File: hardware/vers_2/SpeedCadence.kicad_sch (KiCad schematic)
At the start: 30 parts, among them J1 Conn_ST_STDC14, J2 USB_C_Receptacle_USB2.0_16P, J3 Conn_01x03_Pin, J4 Conn_01x02_Pin, J5 Conn_01x04_Pin, SW2 SW_Push, U1 AP2112K-3.3, U2 STM32F103C8Tx, U3 TCAN3414DR, Y1 CSTNE8M00G52Z000R0

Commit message: Revision 2
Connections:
- net OLED_SCL: no longer U2.43 (PB7)
- net OLED_SDA: now also U2.43 (PB7)
- net +5V renamed +LDO_IN
- net +5V_BATT renamed GND
- net GND: no longer BT1.1 (Pin_1), D3.2 (A)
- new net +V_BATT: BT1.1 (Pin_1), D3.2 (A)
- no-connect marks 10 -> 34
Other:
- moved on the sheet: BT1, D1, D2, D3, F1, J2, J3, R1, R2

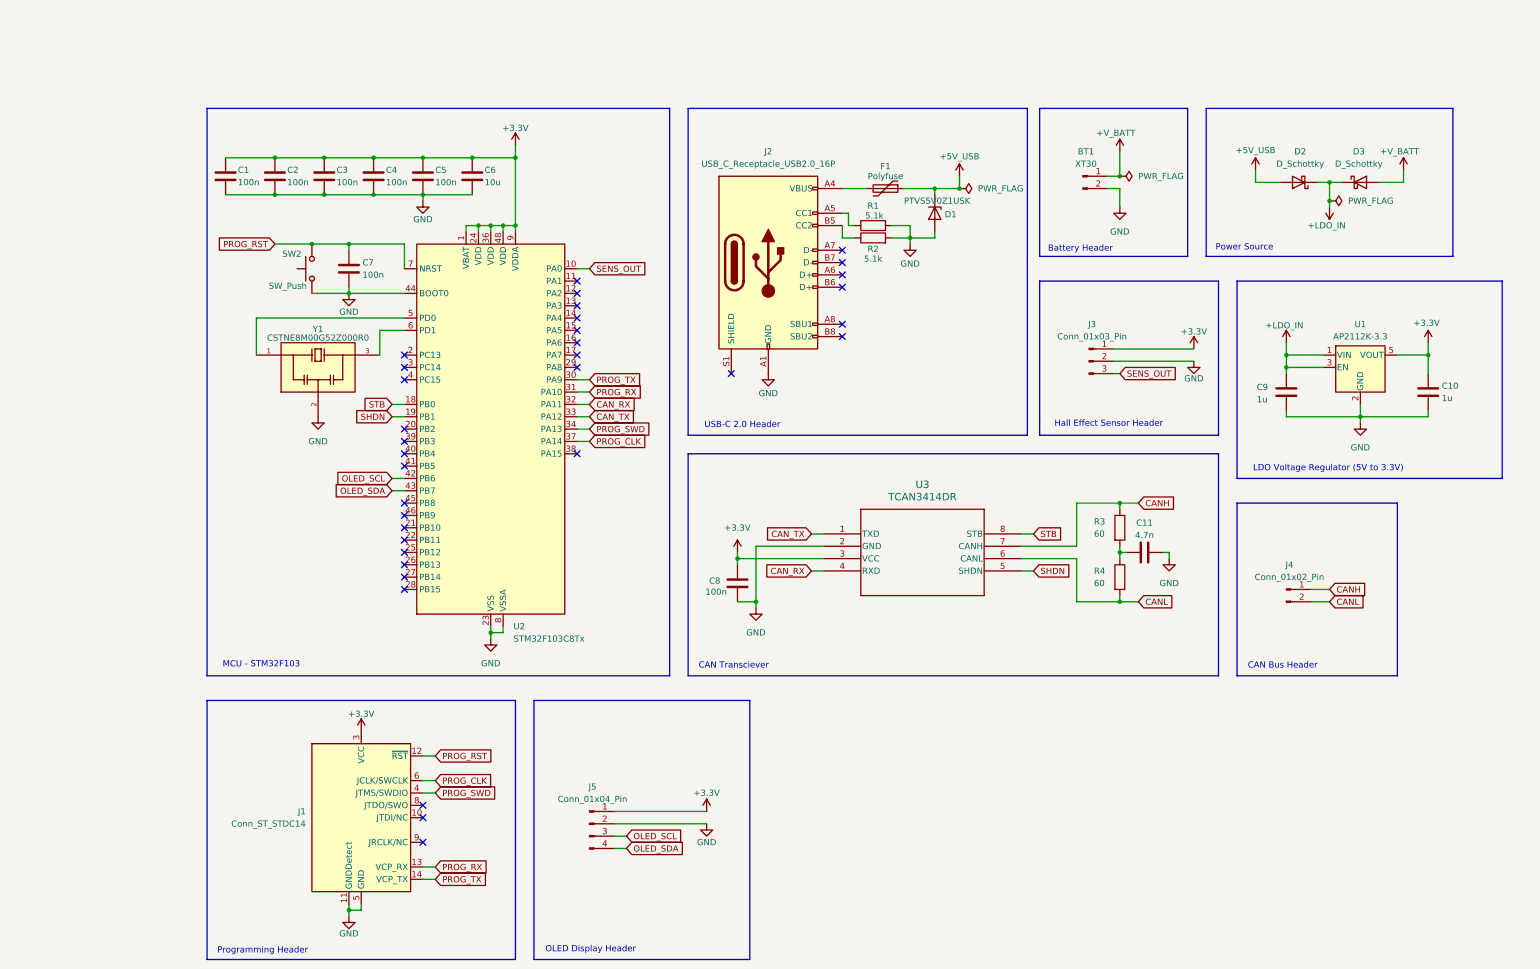
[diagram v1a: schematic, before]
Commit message: Updated LDO
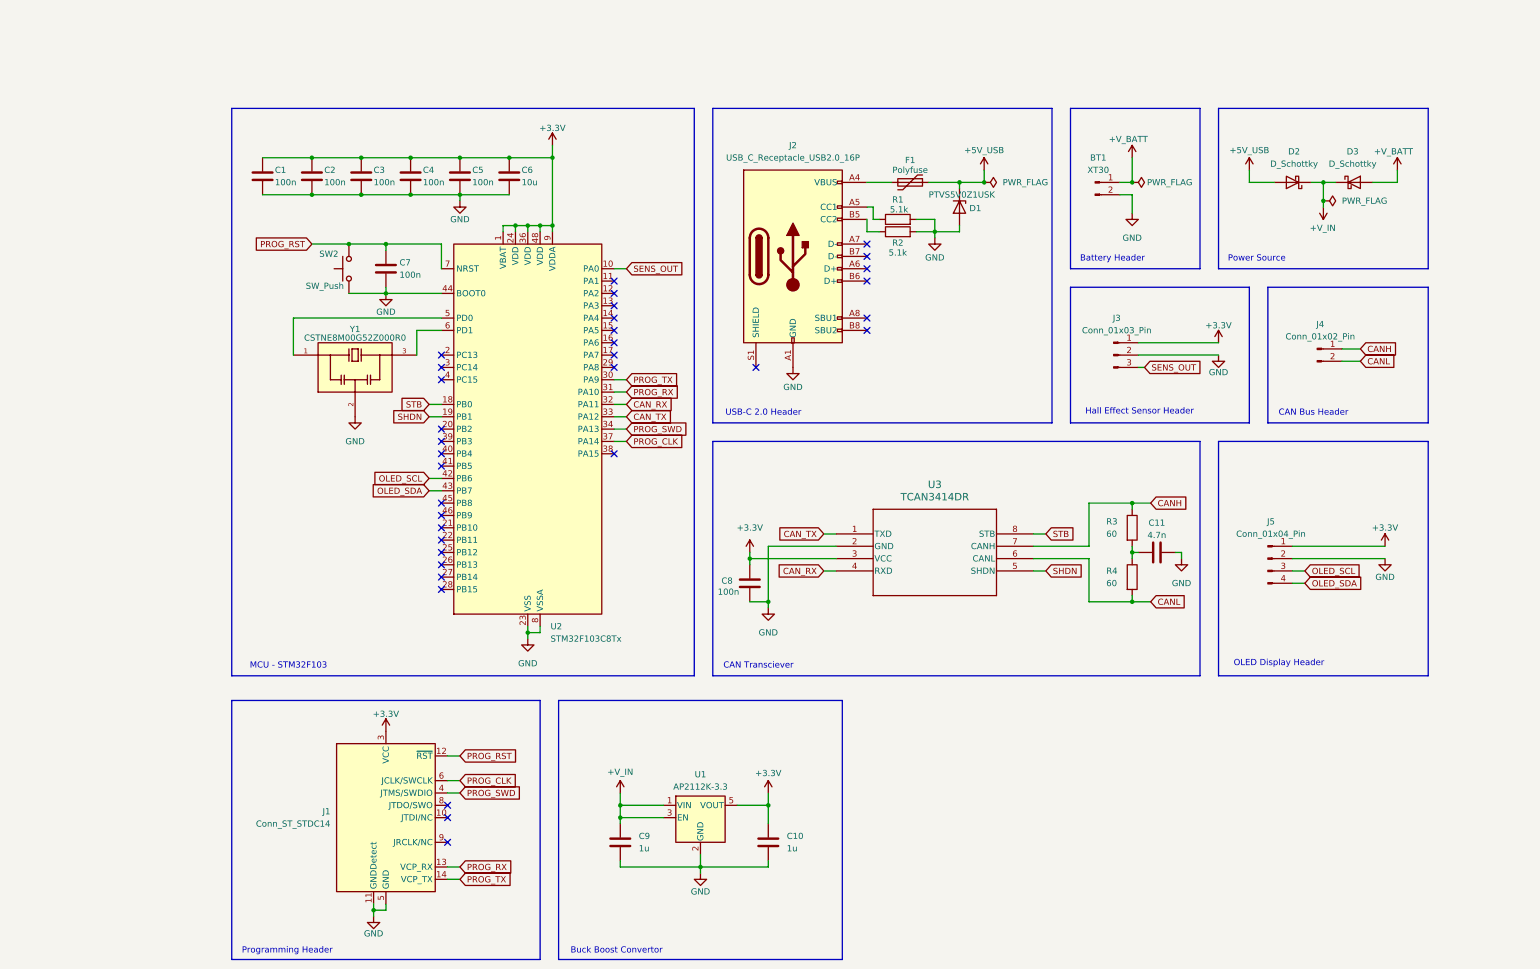
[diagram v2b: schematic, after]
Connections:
- net +LDO_IN renamed +V_IN
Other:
- note added: "Buck Boost Convertor"
- note removed: "LDO Voltage Regulator (5V to 3.3V)"
- moved on the sheet: BT1, C1, C11, C2, C3, C4, C5, C6, C7, C8, D1, D2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

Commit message: PCB design complete
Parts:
- removed C1: 100n, Capacitor_SMD:C_0805_2012Metric, symbol Device:C
- added H1, H2, H3, H4: MountingHole, MountingHole:MountingHole_2.2mm_M2, symbol Mechanical:MountingHole
- added R5, R6: 4.7k, Resistor_SMD:R_0805_2012Metric, symbol Device:R
- J6: renamed from BT1; value XT30 -> Conn_01x02_Pin; footprint Connector_AMASS:AMASS_XT30PW-M_1x02_P2.50mm_Horizontal -> Connector_JST:JST_PH_B2B-PH-K_1x02_P2.00mm_Vertical
- renumbered C2 to C1, C11 to C10, C3 to C2, C4 to C3, C5 to C4, C6 to C5, C7 to C6, C8 to C7, C9 to C8, C10 to C9
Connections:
- net +3.3V: now also R5.1, R6.1
- net OLED_SCL: now also R5.2
- net OLED_SDA: now also R6.2
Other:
- note added: "LDO Voltage Regulator"
- note added: "Mounting Holes"
- note removed: "Buck Boost Convertor"
- moved on the sheet: D2, D3, J5, J6

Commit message: Comments for vers2
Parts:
- added R7: R, symbol Device:R
- added SW3: SW_Push, Button_Switch_SMD:SW_SPST_SKQG_WithStem, symbol Switch:SW_Push
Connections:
- net +3.3V: now also SW3.2
- net GND: now also R7.2
- new net BOOT0: R7.1, SW3.1

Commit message: Fixed minor changes
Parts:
- removed R7: R, symbol Device:R
- added R8: 10k, Resistor_SMD:R_0805_2012Metric, symbol Device:R
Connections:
- net +V_BATT: now also J6.2 (Pin_2); no longer J6.1 (Pin_1)
- net GND: now also J6.1 (Pin_1), R8.2; no longer J6.2 (Pin_2), U2.44 (BOOT0)
- net SENS_OUT: now also U2.11 (PA1); no longer U2.10 (PA0)
- net BOOT0: no longer names the net of SW3.1
- net BOOT0: now also U2.44 (BOOT0), R8.1
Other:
- moved on the sheet: C1, C2, C3, C4, C5, C6, J6, SW2, U2

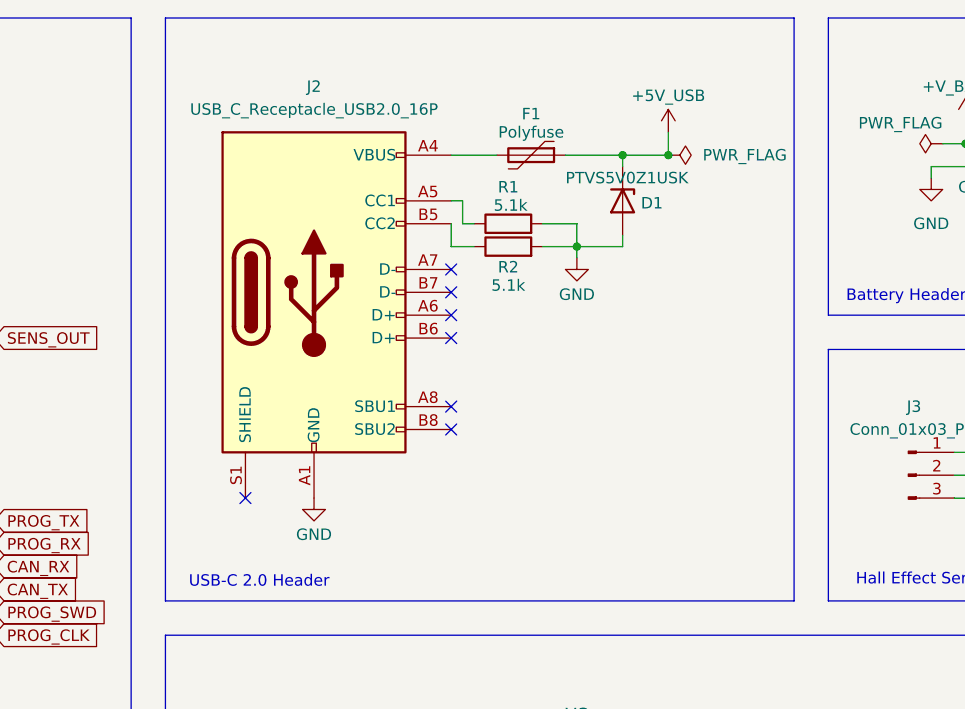
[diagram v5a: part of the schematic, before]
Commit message: removed tvs diode
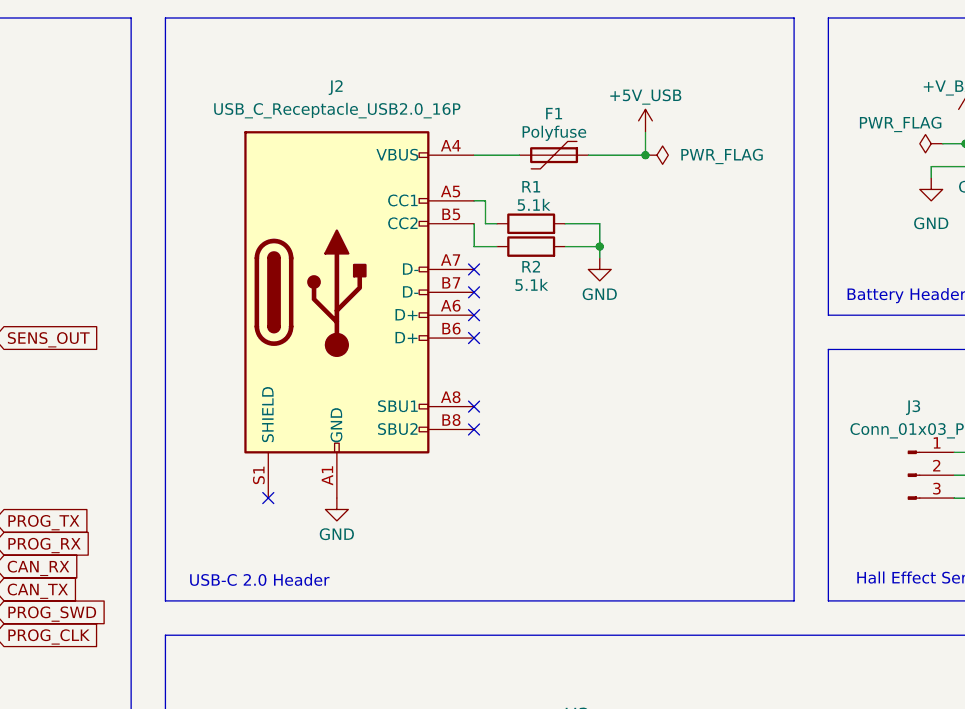
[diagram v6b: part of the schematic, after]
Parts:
- removed D1: PTVS5V0Z1USK, Diode_SMD:Nexperia_DSN1608-2_1.6x0.8mm, symbol Diode:PTVS5V0Z1USK
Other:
- moved on the sheet: F1, J2, R1, R2

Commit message: R3, R4 changed to 0603 footprint
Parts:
- R1: footprint Resistor_SMD:R_0805_2012Metric -> Capacitor_SMD:C_0603_1608Metric
- R3, R4: footprint Resistor_SMD:R_0805_2012Metric -> Resistor_SMD:R_0603_1608Metric
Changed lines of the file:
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@@
 			)
 		)
-		(property "Footprint" "Resistor_SMD:R_0805_2012Metric"
+		(property "Footprint" "Resistor_SMD:R_0603_1608Metric"
 			(at 201.422 113.03 90)
 			(effects
@@
 			)
 		)
-		(property "Footprint" "Resistor_SMD:R_0805_2012Metric"
+		(property "Footprint" "Capacitor_SMD:C_0603_1608Metric"
 			(at 157.48 41.148 90)
 			(effects
@@
 			)
 		)
-		(property "Footprint" "Resistor_SMD:R_0805_2012Metric"
+		(property "Footprint" "Resistor_SMD:R_0603_1608Metric"
 			(at 201.422 102.87 90)
 			(effects

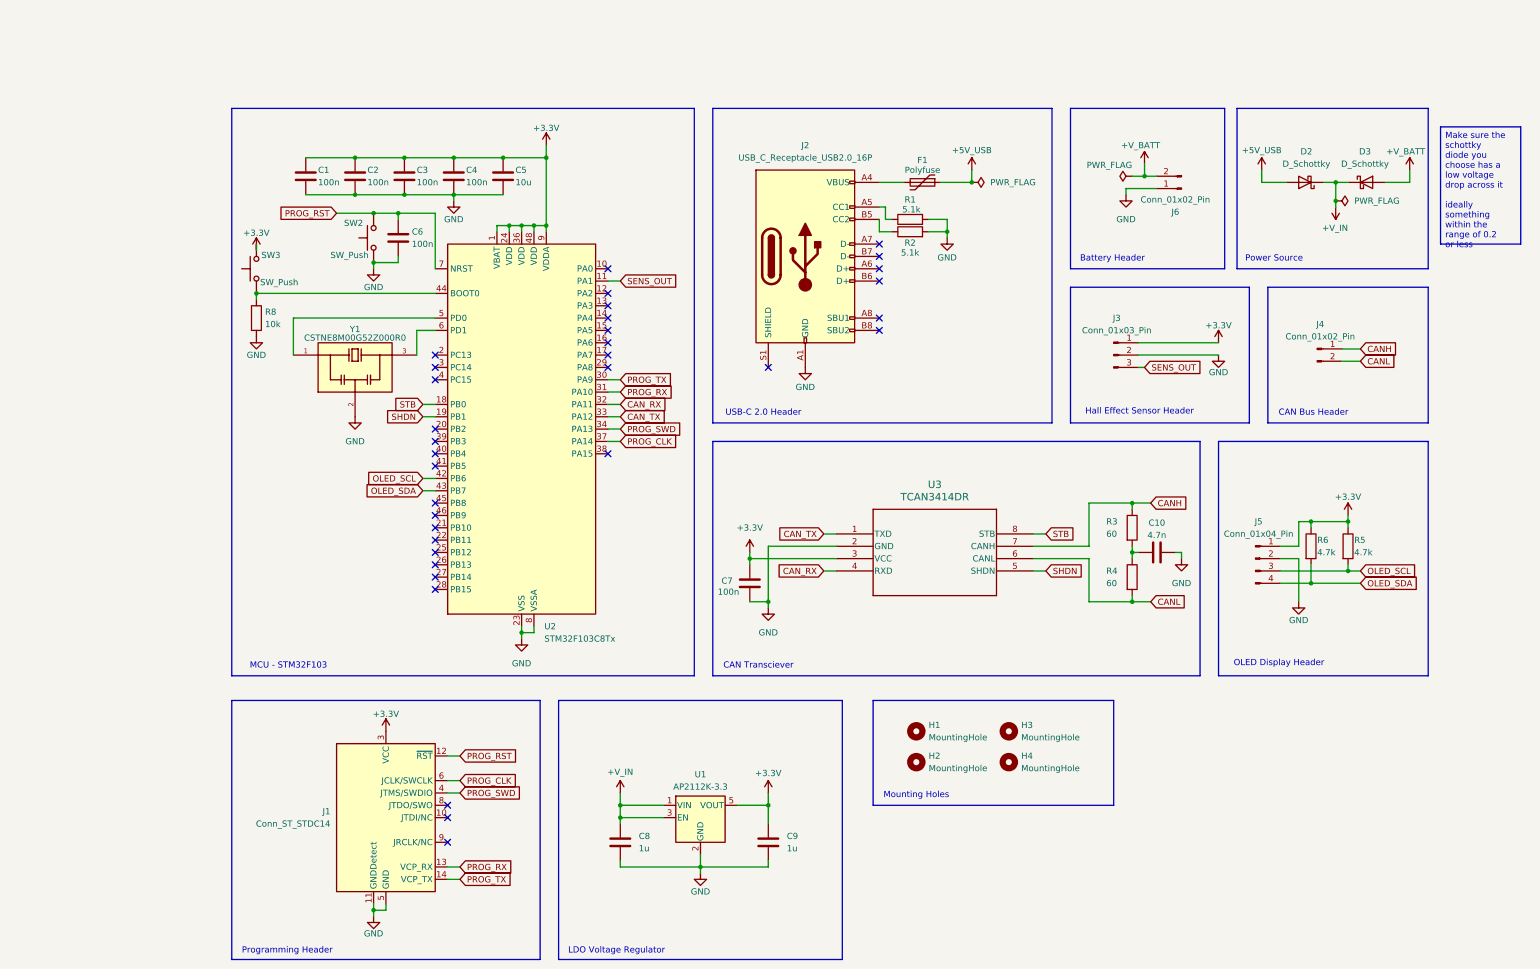
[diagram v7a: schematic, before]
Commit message: Changed to 6.4V with buck converter
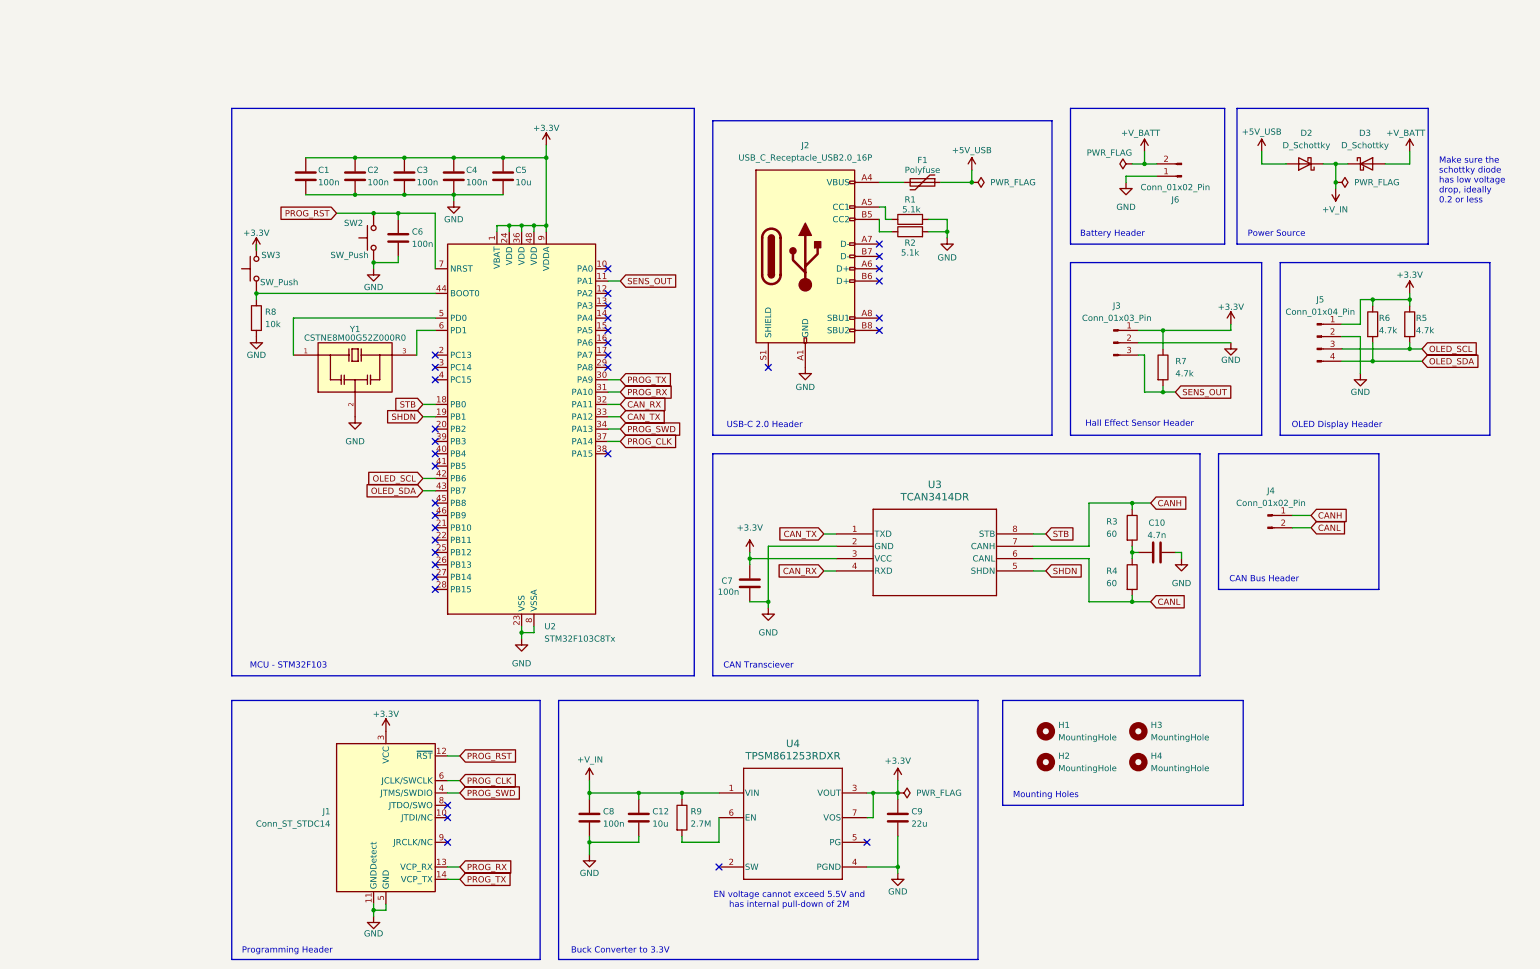
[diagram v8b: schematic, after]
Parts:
- removed U1: AP2112K-3.3, Package_TO_SOT_SMD:SOT-23-5, symbol Regulator_Linear:AP2112K-3.3
- added C12: 10u, Capacitor_SMD:C_0805_2012Metric, symbol Device:C
- added R7: 4.7k, Resistor_SMD:R_0805_2012Metric, symbol Device:R
- added R9: 2.7M, Resistor_SMD:R_0805_2012Metric, symbol Device:R
- added U4: TPSM861253RDXR, TPSM861253:VREG_TPSM861253RDXR, symbol TPSM861253:TPSM861253RDXR
- C8: value 1u -> 100n
- C9: value 1u -> 22u
- J6: footprint Connector_JST:JST_PH_B2B-PH-K_1x02_P2.00mm_Vertical -> Connector_JST:JST_XH_B2B-XH-A_1x02_P2.50mm_Vertical
- R1: footprint Capacitor_SMD:C_0603_1608Metric -> Resistor_SMD:R_0805_2012Metric
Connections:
- net +3.3V: now also R7.1, U4.3 (VOUT), U4.7 (VOS)
- net +V_IN: now also C12.1, R9.1, U4.1 (VIN)
- net GND: now also C12.2, U4.4 (PGND)
- net SENS_OUT: now also R7.2
- new net: R9.2, U4.6 (EN)
- no-connect marks 34 -> 36
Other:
- note added: "Buck Converter to 3.3V"
- note added: "EN voltage cannot exceed 5.5V and has internal pull-down of 2M"
- note removed: "LDO Voltage Regulator"
- moved on the sheet: D2, D3, H1, H2, H3, H4, J3, J4, J5, J6, R5, R6
